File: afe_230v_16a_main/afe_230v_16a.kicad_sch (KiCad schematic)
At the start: 72 parts, among them J4 MCV 1,5/ 6-G-3,81, P1 06-14-03_rectifier, U1 ${SIM.PARAMS}, U17 1_element_2_current, U2 AD8538, U20 watt_hour_meter_bidirectional, U21 3w_ne, U3 AD8538, U4 AQH3223A, U5 ACS711xLCTR-25AB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

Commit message: updated schema
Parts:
- added J5: HBUS16, Connector_PinHeader_2.54mm:PinHeader_2x08_P2.54mm_Vertical, symbol Connector_Generic:Conn_02x08_Odd_Even
- added R38: 0K, Resistor_SMD:R_0805_2012Metric, symbol Device:R
- R30: footprint (none) -> Resistor_SMD:R_0805_2012Metric
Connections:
- net A2: now also R38.1
- net DGND: now also J5.15 (Pin_15)
- net at U20.: now also T16.
- net at T16.: now also T17.; no longer U20.
- net V0_sense: now reaches D3.2 (A), R11.2, R13.1
- net V0_sense: now also J5.1 (Pin_1)
- net V1_sense: now reaches D4.2 (A), R12.2, R14.1
- net V1_sense: now also J5.3 (Pin_3)
- net at C8.: now also T10.
- net at T10.: now also T8.; no longer C8.
- net at C7.: now also C3., P1., T8., U8.
- net at T17.: now also C12.; no longer T16.
- net at T7.: now also C3.
- net at T11.: now also C9.; no longer T9.
- net at C9.: no longer T11.
- net at U21.: no longer C12.
- new net: T11., T9.
- new net: C12., U21.
- new net 24V: J5.13 (Pin_13)
- new net CAN_hi: J5.9 (Pin_9)
- new net CAN_lo: J5.11 (Pin_11)
- new net I0_sense: J5.8 (Pin_8), R38.2
- new net K0_on: J5.5 (Pin_5)
- new net K0_status: J5.7 (Pin_7)
- new net K1_on: J5.10 (Pin_10)
- new net K1_status: J5.12 (Pin_12)
- new net K2_on: J5.14 (Pin_14)
- new net K2_status: J5.16 (Pin_16)
- new net V2_sense: J5.2 (Pin_2)
- new net V3_sense: J5.4 (Pin_4)
- new net V4_sense: J5.6 (Pin_6)
- now unconnected: P1., U8.
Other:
- note added: "Note: AMC1200 may allow high side"

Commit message: began PCBA layout
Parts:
- J5: footprint Connector_PinHeader_2.54mm:PinHeader_2x08_P2.54mm_Vertical -> Connector_PinHeader_2.54mm:PinHeader_2x09_P2.54mm_Vertical; symbol Connector_Generic:Conn_02x08_Odd_Even -> Connector_Generic:Conn_02x09_Odd_Even
- R20, R24, R25, R26, R27, R28: value 1K -> 1K_dnp
- R31, R32, R33, R34, R37: footprint (none) -> Resistor_SMD:R_0805_2012Metric
- R38: value 0K -> 0K_dnp
- U3, U6: value AD8538 -> AD8538_dnp
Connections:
- net 24V: now also J5.15 (Pin_15); no longer J5.13 (Pin_13)
- net CAN_hi: now also J5.11 (Pin_11); no longer J5.9 (Pin_9)
- net CAN_lo: now also J5.13 (Pin_13); no longer J5.11 (Pin_11)
- net DGND: now also J5.17 (Pin_17); no longer J5.15 (Pin_15)
- net K1_on: now also J5.12 (Pin_12); no longer J5.10 (Pin_10)
- net K1_status: now also J5.14 (Pin_14); no longer J5.12 (Pin_12)
- net K2_on: now also J5.16 (Pin_16); no longer J5.14 (Pin_14)
- net K2_status: now also J5.18 (Pin_18); no longer J5.16 (Pin_16)
- net at U20.: now also T16.
- net at T16.: now also T17.; no longer U20.
- net at C8.: now also T10.
- net at T10.: now also T8.; no longer C8.
- net at C7.: now also C3., P1., T8., U8.
- net at T17.: now also C12.; no longer T16.
- net at T7.: now also C3.
- net at T11.: now also C9.; no longer T9.
- net at C9.: no longer T11.
- net at U21.: no longer C12.
- new net: T11., T9.
- new net: C12., U21.
- now unconnected: P1., U8.
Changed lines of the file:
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@@
 	(wire
 		(pts
-			(xy 300.99 46.99) (xy 306.07 46.99)
+			(xy 300.99 49.53) (xy 306.07 49.53)
 		)
 		(stroke
@@
 	(wire
 		(pts
-			(xy 300.99 39.37) (xy 306.07 39.37)
+			(xy 300.99 41.91) (xy 306.07 41.91)
 		)
 		(stroke
@@
 	(wire
 		(pts
-			(xy 300.99 41.91) (xy 306.07 41.91)
+			(xy 300.99 44.45) (xy 306.07 44.45)
 		)
 		(stroke
@@
 	(wire
 		(pts
-			(xy 300.99 44.45) (xy 306.07 44.45)
+			(xy 300.99 46.99) (xy 306.07 46.99)
 		)
 		(stroke
@@
 	(wire
 		(pts
-			(xy 318.77 39.37) (xy 323.85 39.37)
+			(xy 318.77 41.91) (xy 323.85 41.91)
 		)
 		(stroke
@@
 	(wire
 		(pts
-			(xy 318.77 46.99) (xy 323.85 46.99)
+			(xy 318.77 49.53) (xy 323.85 49.53)
 		)
 		(stroke
@@
 	(wire
 		(pts
-			(xy 318.77 41.91) (xy 323.85 41.91)
+			(xy 318.77 44.45) (xy 323.85 44.45)
 		)
 		(stroke
@@
 	(wire
 		(pts
-			(xy 318.77 44.45) (xy 323.85 44.45)
+			(xy 318.77 46.99) (xy 323.85 46.99)
 		)
 		(stroke
@@
 	)
 	(label "K2_status"
-		(at 323.85 46.99 0)
+		(at 323.85 49.53 0)
 		(effects
 			(font
@@
 	)
 	(label "CAN_hi"
-		(at 300.99 39.37 180)
+		(at 300.99 41.91 180)
 		(effects
 			(font
@@
 	)
 	(label "K1_on"
-		(at 323.85 39.37 0)
+		(at 323.85 41.91 0)
 		(effects
 			(font
@@
 	)
 	(label "CAN_lo"
-		(at 300.99 41.91 180)
+		(at 300.99 44.45 180)
 		(effects
 			(font
@@
 	)
 	(label "24V"
-		(at 300.99 44.45 180)
+		(at 300.99 46.99 180)
 		(effects
 			(font
@@
 	)
 	(label "K2_on"
-		(at 323.85 44.45 0)
+		(at 323.85 46.99 0)
 		(effects
 			(font
@@
 	)
 	(label "K1_status"
-		(at 323.85 41.91 0)
+		(at 323.85 44.45 0)
 		(effects
 			(font
@@
 	)
 	(label "DGND"
-		(at 300.99 46.99 180)
+		(at 300.99 49.53 180)
 		(effects
 			(font
@@
 			)
 		)
-		(property "Footprint" ""
+		(property "Footprint" "Resistor_SMD:R_0805_2012Metric"
 			(at 194.31 215.138 90)
 			(effects
@@
 			)
 		)
-		(property "Value" "1K"
+		(property "Value" "1K_dnp"
 			(at 214.63 73.66 90)
 			(effects
@@
 			)
 		)
-		(property "Value" "1K"
+		(property "Value" "1K_dnp"
 			(at 247.65 31.75 90)
 			(effects
@@
 			)
 		)
-		(property "Value" "1K"
+		(property "Value" "1K_dnp"
 			(at 201.93 60.9599 0)
 			(effects
@@
 	)
 	(symbol
-		(lib_id "Connector_Generic:Conn_02x08_Odd_Even")
-		(at 311.15 36.83 0)
+		(lib_id "Connector_Generic:Conn_02x09_Odd_Even")
+		(at 311.15 39.37 0)
 		(unit 1)
 		(exclude_from_sim no)
@@
 			)
 		)
-		(property "Footprint" "Connector_PinHeader_2.54mm:PinHeader_2x08_P2.54mm_Vertical"
-			(at 311.15 36.83 0)
+		(property "Footprint" "Connector_PinHeader_2.54mm:PinHeader_2x09_P2.54mm_Vertical"
+			(at 311.15 39.37 0)
 			(effects
 				(font
@@
 		)
 		(property "Datasheet" "~"
-			(at 311.15 36.83 0)
+			(at 311.15 39.37 0)
 			(effects
 				(font
@@
 			)
 		)
-		(property "Description" "Generic connector, double row, 02x08, odd/even pin numbering scheme (row 1 odd numbers, row 2 even numbers), script generated (kicad-library-utils/schlib/autogen/connector/)"
-			(at 311.15 36.83 0)
+		(property "Description" "Generic connector, double row, 02x09, odd/even pin numbering scheme (row 1 odd numbers, row 2 even numbers), script generated (kicad-library-utils/schlib/autogen/connector/)"
+			(at 311.15 39.37 0)
 			(effects
 				(font
@@
 		(pin "13"
 		)
+		(pin "17"
+		)
+		(pin "18"
+		)
 		(instances
 			(project "afe_230v_16a"
@@
 			)
 		)
-		(property "Value" "AD8538"
+		(property "Value" "AD8538_dnp"
 			(at 173.99 191.516 0)
 			(effects
@@
 			)
 		)
-		(property "Value" "1K"
+		(property "Value" "1K_dnp"
 			(at 234.95 73.66 90)
 			(effects
@@
 			)
 		)
-		(property "Footprint" ""
+		(property "Footprint" "Resistor_SMD:R_0805_2012Metric"
 			(at 173.99 184.658 90)
 			(effects
@@
 			)
 		)
-		(property "Footprint" ""
+		(property "Footprint" "Resistor_SMD:R_0805_2012Metric"
 			(at 143.51 210.058 90)
 			(effects
@@
 			)
 		)
-		(property "Footprint" ""
+		(property "Footprint" "Resistor_SMD:R_0805_2012Metric"
 			(at 214.63 210.058 90)
 			(effects
@@
 			)
 		)
-		(property "Value" "AD8538"
+		(property "Value" "AD8538_dnp"
 			(at 248.92 53.3714 0)
 			(effects
@@
 			)
 		)
-		(property "Value" "1K"
+		(property "Value" "1K_dnp"
 			(at 220.98 31.75 90)
 			(effects
@@
 			)
 		)
-		(property "Footprint" ""
+		(property "Footprint" "Resistor_SMD:R_0805_2012Metric"
 			(at 207.01 199.898 90)
 			(effects
@@
 			)
 		)
-		(property "Value" "0K"
+		(property "Value" "0K_dnp"
 			(at 215.9 176.53 90)
 			(effects
@@
 			)
 		)
-		(property "Value" "1K"
+		(property "Value" "1K_dnp"
 			(at 262.89 53.34 90)
 			(effects

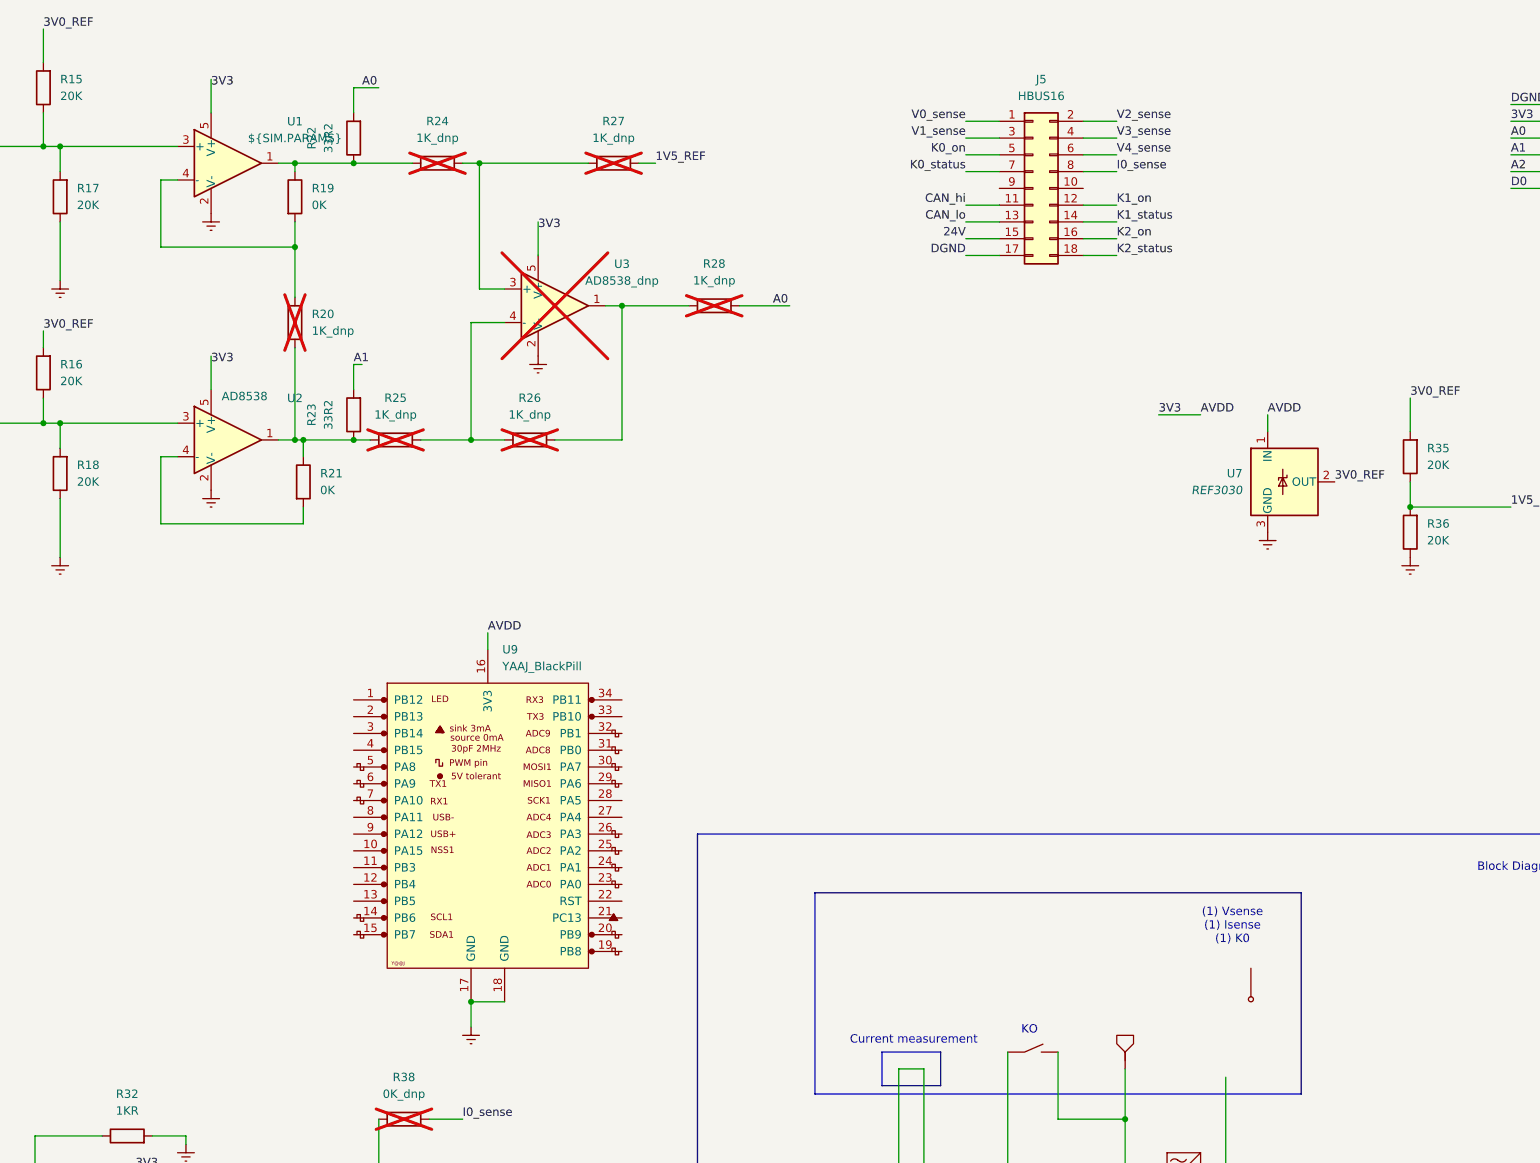
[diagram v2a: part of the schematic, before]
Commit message: added pcb2&3 board outlines, adjusted i/o
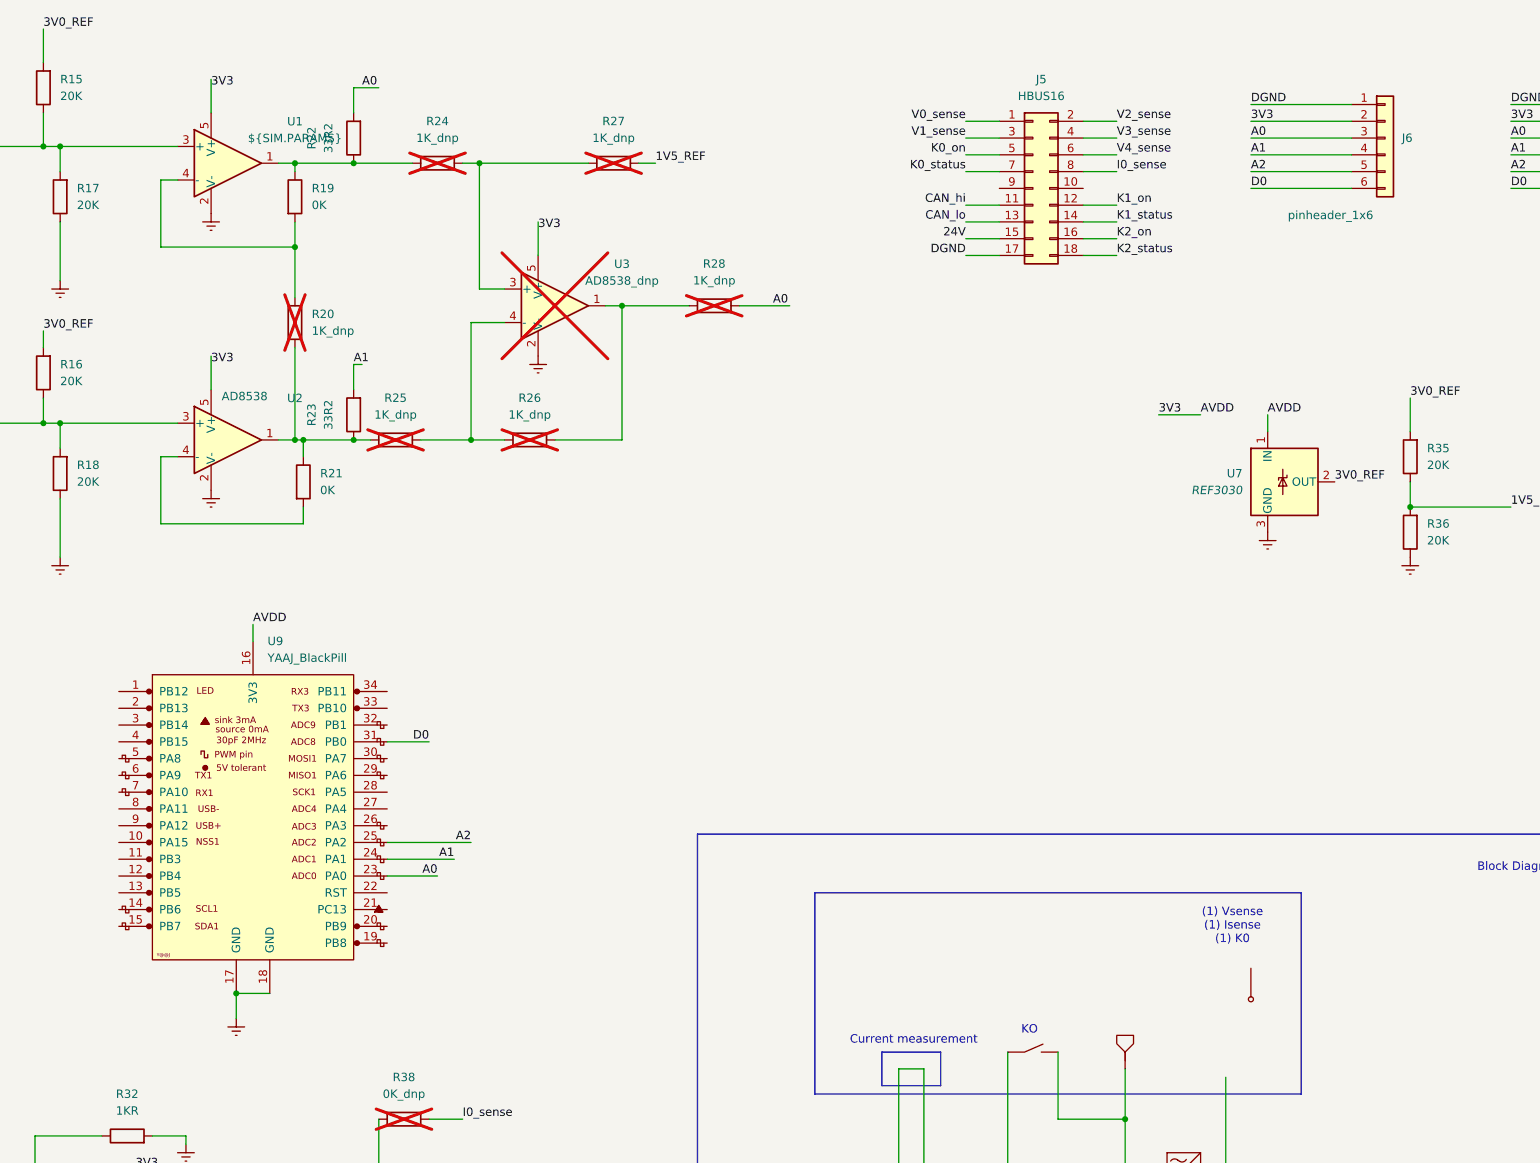
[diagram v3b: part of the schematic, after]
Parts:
- added J6: pinheader_1x6, Connector_PinHeader_2.54mm:PinHeader_1x06_P2.54mm_Vertical, symbol Connector_Generic:Conn_01x06
- D1, D2, D3, D4: footprint Diode_SMD:D_SOD-323F -> Diode_SMD:D_SOD-323_HandSoldering
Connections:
- net 3V3: now also J6.2 (Pin_2)
- net A0: now also U9.23 (PA0), J6.3 (Pin_3)
- net A1: now also U9.24 (PA1), J6.4 (Pin_4)
- net A2: now also U9.25 (PA2), J6.5 (Pin_5)
- net D0: now also U9.31 (PB0), J6.6 (Pin_6)
- net DGND: now also J6.1 (Pin_1)
- net at U20.: now also T16.
- net at T16.: now also T17.; no longer U20.
- net at C8.: now also T10.
- net at T10.: now also T8.; no longer C8.
- net at C7.: now also C3., P1., T8., U8.
- net at T17.: now also C12.; no longer T16.
- net at T7.: now also C3.
- net at T11.: now also C9.; no longer T9.
- net at C9.: no longer T11.
- net at U21.: no longer C12.
- new net: T11., T9.
- new net: C12., U21.
- now unconnected: P1., U8.
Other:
- moved on the sheet: U9
